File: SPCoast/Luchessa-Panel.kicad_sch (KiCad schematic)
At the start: 21 parts, among them SW8784 783, SW8796 795, SW8800 799, U8004 0x24, U8005 0x25, U8006 0x26

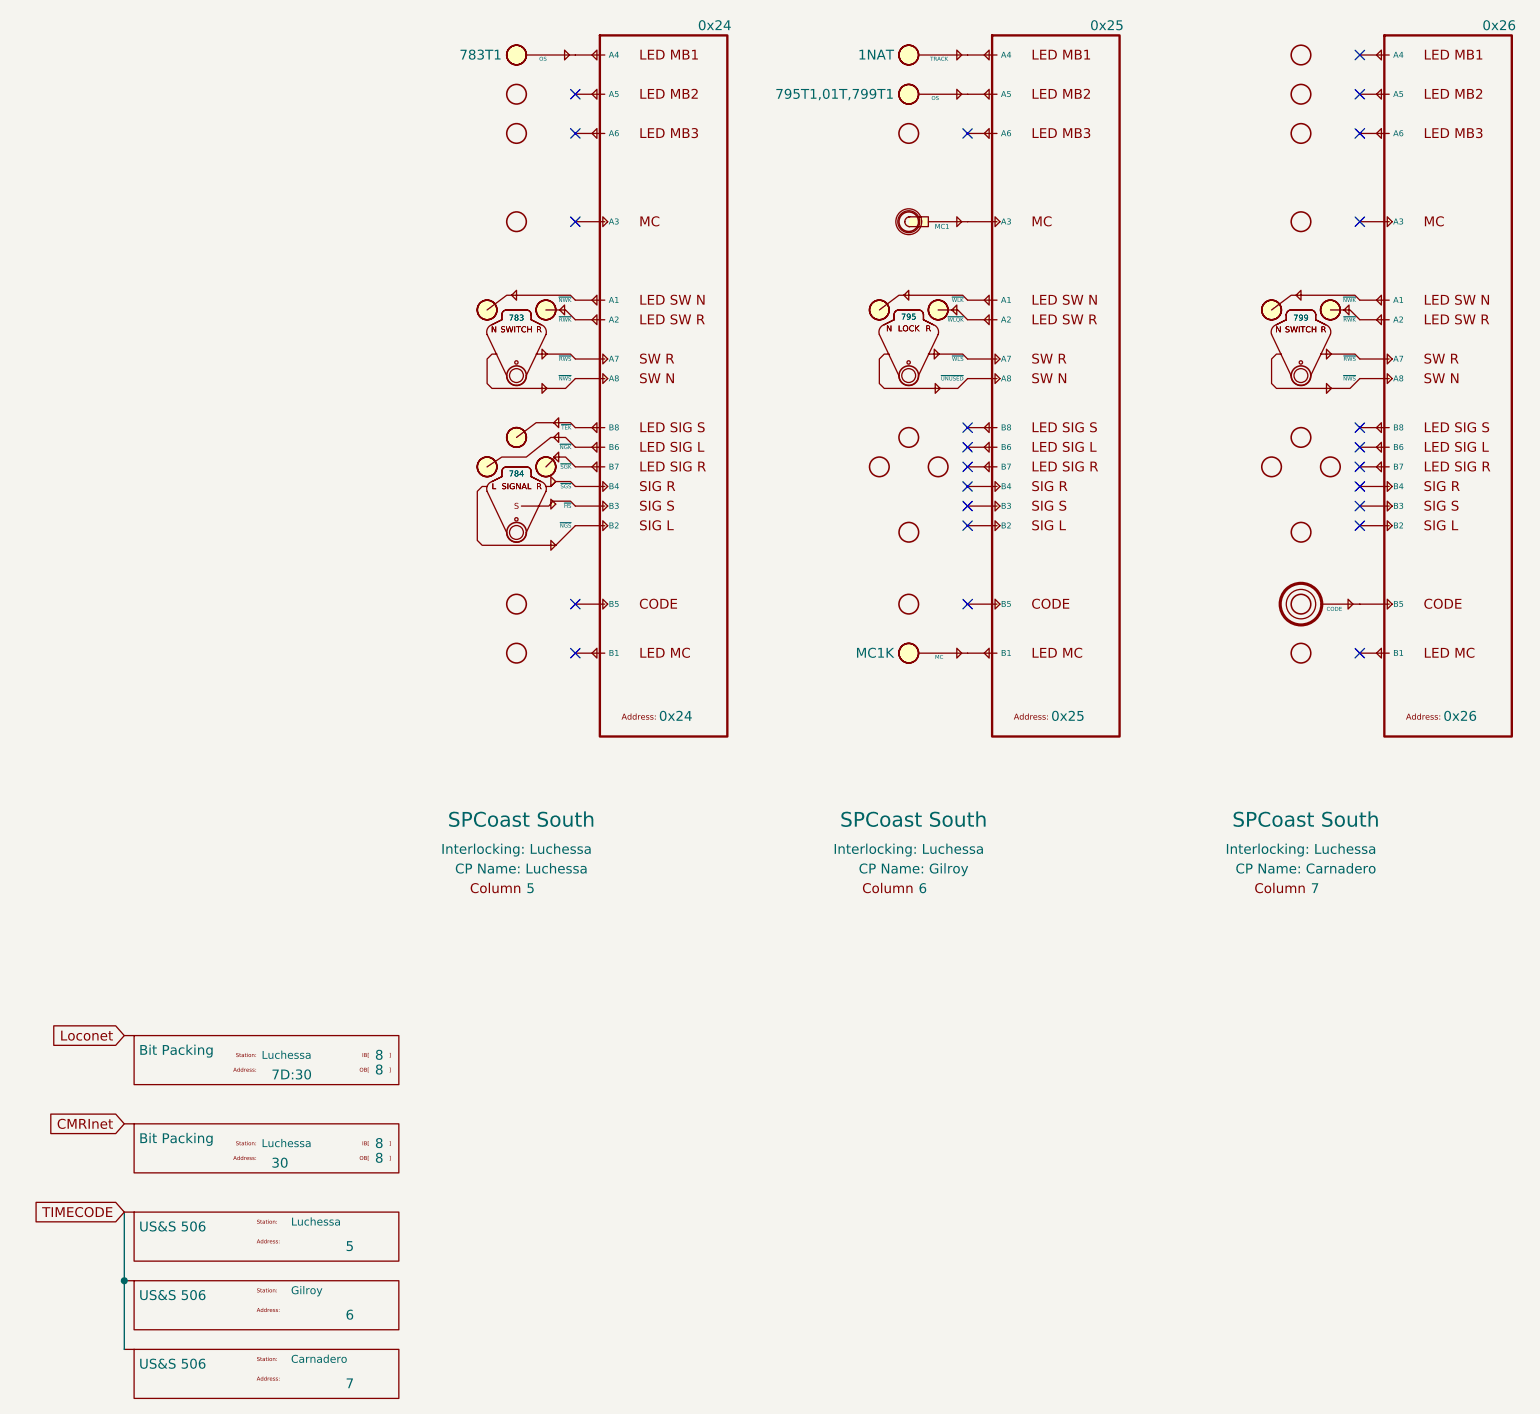
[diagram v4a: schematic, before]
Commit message: chore(kicad): owner edits: GPIO drivers carry Address, Sargent I2C addresses, CMRI body text from fields
Baseline of the owner's saved work before the ADR 0005 scripts:
- Driver-GPIO-Digital and Driver-GPIO-Pixel gain an Address field (the
  board pin); Value renders ${Address}; body text and arrow adjusted.
- Driver-CMRI-IB/OB body text renders UA${Address}.IN/OUT.${Bit} from
  the fields instead of ${VALUE}.
- Sargent, Gilroy Interchange and Luchessa GPIO instances carry Address;
  Sargent Exp2 back at 0x26, Exp3 0x27.
- All sheets resaved by KiCad 10 (reordering), project file
  used_designators cleared by KiCad.

Verified: no lock files; committed as saved, unverified by netlist (the
baseline netlist is exported in the next step).

Co-Authored-By: Claude Fable 5.1 <noreply@anthropic.com>
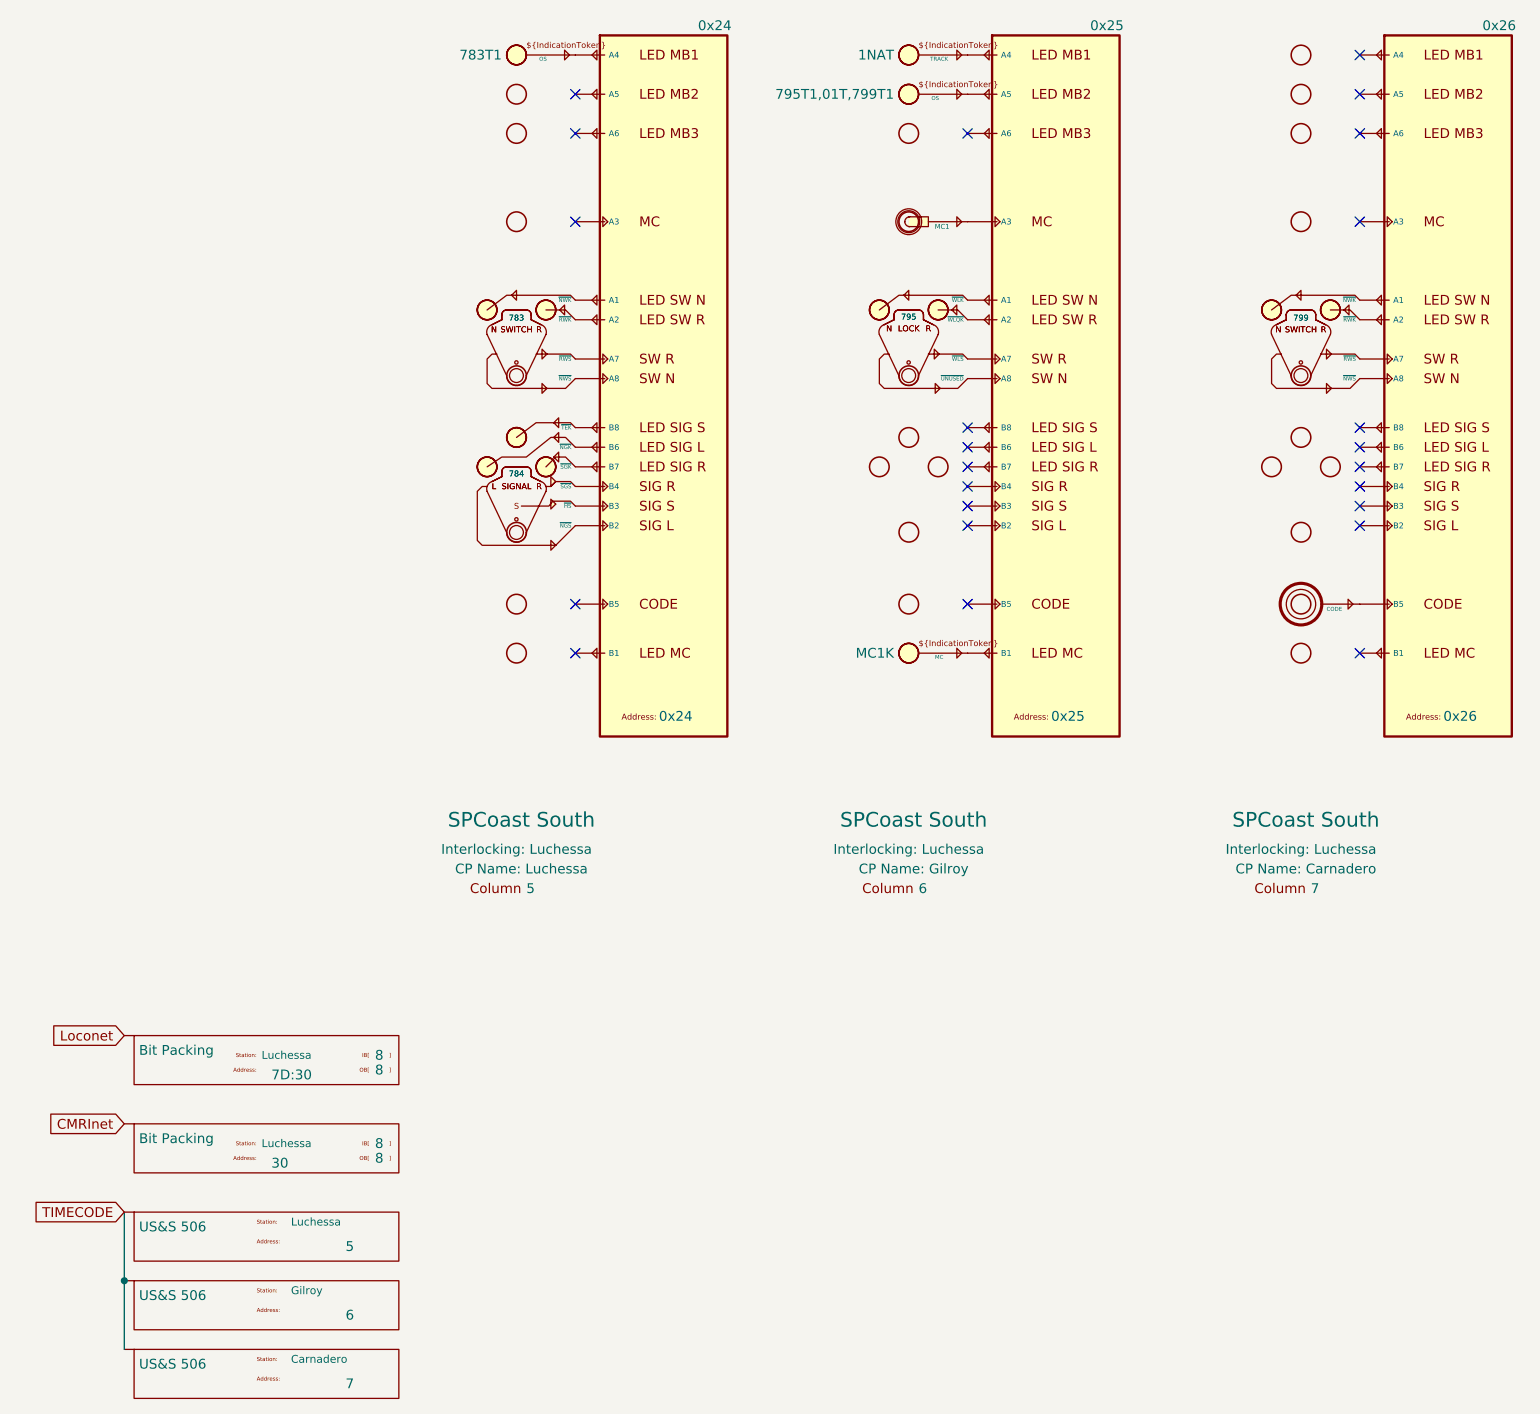
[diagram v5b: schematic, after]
